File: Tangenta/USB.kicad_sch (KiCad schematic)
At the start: 29 parts, among them J12 907-211A1019D10200, J13 906-151A1058D10200, U8 USB2514B-I_M2, X1 X322524MOB4SI

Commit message: Libraries exported from global to project.
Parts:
- C1: symbol Device:C_Small -> CholaSymbolsPrjLib:C_Small
- C48, C49: symbol CAP_L5:16CE47FSS -> CholaSymbolsPrjLib:16CE47FSS
- FB1: symbol Ferrite_Bead_100:GZ2012D101TF -> CholaSymbolsPrjLib:GZ2012D101TF
- J12: symbol USB_2_CONNECTOR:907-211A1019D10200 -> CholaSymbolsPrjLib:907-211A1019D10200
- J13: symbol USB_VERTICAL_BLUE:906-151A1058D10200 -> CholaSymbolsPrjLib:906-151A1058D10200
- R2: symbol Device:R_Small_US -> CholaSymbolsPrjLib:R_Small_US
- U8: symbol USB_HUB:USB2514B-I_M2 -> CholaSymbolsPrjLib:USB2514B-I_M2
- X1: symbol XTAL_24MHZ:X322524MOB4SI -> CholaSymbolsPrjLib:X322524MOB4SI
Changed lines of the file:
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@@
     (effects (font (size 1.27 1.27)) (justify right))
   )
-  (symbol (lib_id "Device:R_Small_US") (at 184.15 97.79 270) (mirror x) (unit 1)
+  (symbol (lib_id "CholaSymbolsPrjLib:R_Small_US") (at 184.15 97.79 270) (mirror x) (unit 1)
     (in_bom yes) (on_board yes) (dnp no)
     (property "Reference" "R2" (at 186.055 96.52 90)
@@
     )
   )
-  (symbol (lib_id "Device:C_Small") (at 62.611 168.91 180) (unit 1)
+  (symbol (lib_id "CholaSymbolsPrjLib:C_Small") (at 62.611 168.91 180) (unit 1)
     (in_bom yes) (on_board yes) (dnp no)
     (property "Reference" "C1" (at 60.452 167.386 0)
@@
     )
   )
-  (symbol (lib_id "Device:C_Small") (at 38.862 168.91 180) (unit 1)
+  (symbol (lib_id "CholaSymbolsPrjLib:C_Small") (at 38.862 168.91 180) (unit 1)
     (in_bom yes) (on_board yes) (dnp no)
     (property "Reference" "C1" (at 36.703 167.386 0)
@@
     )
   )
-  (symbol (lib_id "Device:C_Small") (at 55.118 168.91 180) (unit 1)
+  (symbol (lib_id "CholaSymbolsPrjLib:C_Small") (at 55.118 168.91 180) (unit 1)
     (in_bom yes) (on_board yes) (dnp no)
     (property "Reference" "C1" (at 52.959 167.386 0)
@@
     )
   )
-  (symbol (lib_id "XTAL_24MHZ:X322524MOB4SI") (at 104.775 166.37 180) (unit 1)
+  (symbol (lib_id "CholaSymbolsPrjLib:X322524MOB4SI") (at 104.775 166.37 180) (unit 1)
     (in_bom yes) (on_board yes) (dnp no)
     (property "Reference" "X1" (at 104.775 160.02 0)
@@
     )
   )
-  (symbol (lib_id "Device:C_Small") (at 46.355 168.91 180) (unit 1)
+  (symbol (lib_id "CholaSymbolsPrjLib:C_Small") (at 46.355 168.91 180) (unit 1)
     (in_bom yes) (on_board yes) (dnp no)
     (property "Reference" "C1" (at 44.196 167.386 0)
@@
     )
   )
-  (symbol (lib_id "Device:C_Small") (at 95.25 180.34 180) (unit 1)
+  (symbol (lib_id "CholaSymbolsPrjLib:C_Small") (at 95.25 180.34 180) (unit 1)
     (in_bom yes) (on_board yes) (dnp no)
     (property "Reference" "C1" (at 99.06 180.34 0)
@@
     )
   )
-  (symbol (lib_id "Device:C_Small") (at 33.655 66.04 180) (unit 1)
+  (symbol (lib_id "CholaSymbolsPrjLib:C_Small") (at 33.655 66.04 180) (unit 1)
     (in_bom yes) (on_board yes) (dnp no)
     (property "Reference" "C1" (at 36.195 64.135 0)
@@
     )
   )
-  (symbol (lib_id "Device:R_Small_US") (at 60.96 77.47 90) (unit 1)
+  (symbol (lib_id "CholaSymbolsPrjLib:R_Small_US") (at 60.96 77.47 90) (unit 1)
     (in_bom yes) (on_board yes) (dnp no)
     (property "Reference" "R2" (at 59.055 76.2 90)
@@
     )
   )
-  (symbol (lib_id "USB_HUB:USB2514B-I_M2") (at 118.1101 76.2 0) (mirror y) (unit 1)
+  (symbol (lib_id "CholaSymbolsPrjLib:USB2514B-I_M2") (at 118.1101 76.2 0) (mirror y) (unit 1)
     (in_bom yes) (on_board yes) (dnp no)
     (property "Reference" "U8" (at 74.93 50.165 0)
@@
     )
   )
-  (symbol (lib_id "Device:R_Small_US") (at 60.96 100.33 90) (unit 1)
+  (symbol (lib_id "CholaSymbolsPrjLib:R_Small_US") (at 60.96 100.33 90) (unit 1)
     (in_bom yes) (on_board yes) (dnp no)
     (property "Reference" "R2" (at 59.182 99.06 90)
@@
     )
   )
-  (symbol (lib_id "Device:C_Small") (at 206.375 93.98 180) (unit 1)
+  (symbol (lib_id "CholaSymbolsPrjLib:C_Small") (at 206.375 93.98 180) (unit 1)
     (in_bom yes) (on_board yes) (dnp no)
     (property "Reference" "C1" (at 208.915 92.075 0)
@@
     )
   )
-  (symbol (lib_id "Device:R_Small_US") (at 60.96 95.25 90) (unit 1)
+  (symbol (lib_id "CholaSymbolsPrjLib:R_Small_US") (at 60.96 95.25 90) (unit 1)
     (in_bom yes) (on_board yes) (dnp no)
     (property "Reference" "R2" (at 59.182 93.98 90)
@@
     )
   )
-  (symbol (lib_id "USB_2_CONNECTOR:907-211A1019D10200") (at 268.605 64.77 0) (unit 1)
+  (symbol (lib_id "CholaSymbolsPrjLib:907-211A1019D10200") (at 268.605 64.77 0) (unit 1)
     (in_bom yes) (on_board yes) (dnp no)
     (property "Reference" "J12" (at 258.445 50.165 0)
@@
     )
   )
-  (symbol (lib_id "Device:R_Small_US") (at 183.515 87.63 270) (mirror x) (unit 1)
+  (symbol (lib_id "CholaSymbolsPrjLib:R_Small_US") (at 183.515 87.63 270) (mirror x) (unit 1)
     (in_bom yes) (on_board yes) (dnp no)
     (property "Reference" "R2" (at 185.42 86.36 90)
@@
     )
   )
-  (symbol (lib_id "Device:C_Small") (at 114.3 180.34 180) (unit 1)
+  (symbol (lib_id "CholaSymbolsPrjLib:C_Small") (at 114.3 180.34 180) (unit 1)
     (in_bom yes) (on_board yes) (dnp no)
     (property "Reference" "C1" (at 110.49 180.34 0)
@@
     )
   )
-  (symbol (lib_id "Ferrite_Bead_100:GZ2012D101TF") (at 50.673 163.83 0) (unit 1)
+  (symbol (lib_id "CholaSymbolsPrjLib:GZ2012D101TF") (at 50.673 163.83 0) (unit 1)
     (in_bom yes) (on_board yes) (dnp no)
     (property "Reference" "FB1" (at 50.673 161.29 0)
@@
     )
   )
-  (symbol (lib_id "USB_VERTICAL_BLUE:906-151A1058D10200") (at 266.7 93.98 0) (unit 1)
+  (symbol (lib_id "CholaSymbolsPrjLib:906-151A1058D10200") (at 266.7 93.98 0) (unit 1)
     (in_bom yes) (on_board yes) (dnp no)
     (property "Reference" "J13" (at 260.35 85.09 0)
@@
     )
   )
-  (symbol (lib_id "CAP_L5:16CE47FSS") (at 62.103 187.071 0) (unit 1)
+  (symbol (lib_id "CholaSymbolsPrjLib:16CE47FSS") (at 62.103 187.071 0) (unit 1)
     (in_bom yes) (on_board yes) (dnp no)
     (property "Reference" "C48" (at 62.357 185.42 0)
@@
     )
   )
-  (symbol (lib_id "Device:R_Small_US") (at 105.41 177.8 90) (unit 1)
+  (symbol (lib_id "CholaSymbolsPrjLib:R_Small_US") (at 105.41 177.8 90) (unit 1)
     (in_bom yes) (on_board yes) (dnp no)
     (property "Reference" "R2" (at 103.505 176.53 90)
@@
     )
   )
-  (symbol (lib_id "CAP_L5:16CE47FSS") (at 70.104 187.071 0) (unit 1)
+  (symbol (lib_id "CholaSymbolsPrjLib:16CE47FSS") (at 70.104 187.071 0) (unit 1)
     (in_bom yes) (on_board yes) (dnp no)
     (property "Reference" "C49" (at 70.358 185.42 0)
@@
     )
   )
-  (symbol (lib_id "Device:C_Small") (at 201.295 93.98 180) (unit 1)
+  (symbol (lib_id "CholaSymbolsPrjLib:C_Small") (at 201.295 93.98 180) (unit 1)
     (in_bom yes) (on_board yes) (dnp no)
     (property "Reference" "C1" (at 198.755 92.075 0)
@@
     )
   )
-  (symbol (lib_id "Device:C_Small") (at 70.104 168.91 180) (unit 1)
+  (symbol (lib_id "CholaSymbolsPrjLib:C_Small") (at 70.104 168.91 180) (unit 1)
     (in_bom yes) (on_board yes) (dnp no)
     (property "Reference" "C1" (at 67.945 167.386 0)
@@
     )
   )
-  (symbol (lib_id "Device:C_Small") (at 43.815 86.36 180) (unit 1)
+  (symbol (lib_id "CholaSymbolsPrjLib:C_Small") (at 43.815 86.36 180) (unit 1)
     (in_bom yes) (on_board yes) (dnp no)
     (property "Reference" "C1" (at 40.005 85.725 0)
@@
     )
   )
-  (symbol (lib_id "Device:C_Small") (at 28.575 66.04 180) (unit 1)
+  (symbol (lib_id "CholaSymbolsPrjLib:C_Small") (at 28.575 66.04 180) (unit 1)
     (in_bom yes) (on_board yes) (dnp no)
     (property "Reference" "C1" (at 26.035 64.135 0)
@@
     )
   )
-  (symbol (lib_id "Device:R_Small_US") (at 60.96 59.69 90) (unit 1)
+  (symbol (lib_id "CholaSymbolsPrjLib:R_Small_US") (at 60.96 59.69 90) (unit 1)
     (in_bom yes) (on_board yes) (dnp no)
     (property "Reference" "R2" (at 59.055 58.42 90)
@@
     )
   )
-  (symbol (lib_id "Device:R_Small_US") (at 60.96 85.09 90) (unit 1)
+  (symbol (lib_id "CholaSymbolsPrjLib:R_Small_US") (at 60.96 85.09 90) (unit 1)
     (in_bom yes) (on_board yes) (dnp no)
     (property "Reference" "R2" (at 59.055 83.82 90)
@@
     )
   )
-  (symbol (lib_id "Device:R_Small_US") (at 40.005 82.55 90) (unit 1)
+  (symbol (lib_id "CholaSymbolsPrjLib:R_Small_US") (at 40.005 82.55 90) (unit 1)
     (in_bom yes) (on_board yes) (dnp no)
     (property "Reference" "R2" (at 38.1 81.28 90)
@@
     )
   )
-  (symbol (lib_id "Device:C_Small") (at 31.369 168.91 180) (unit 1)
+  (symbol (lib_id "CholaSymbolsPrjLib:C_Small") (at 31.369 168.91 180) (unit 1)
     (in_bom yes) (on_board yes) (dnp no)
     (property "Reference" "C1" (at 29.21 167.386 0)

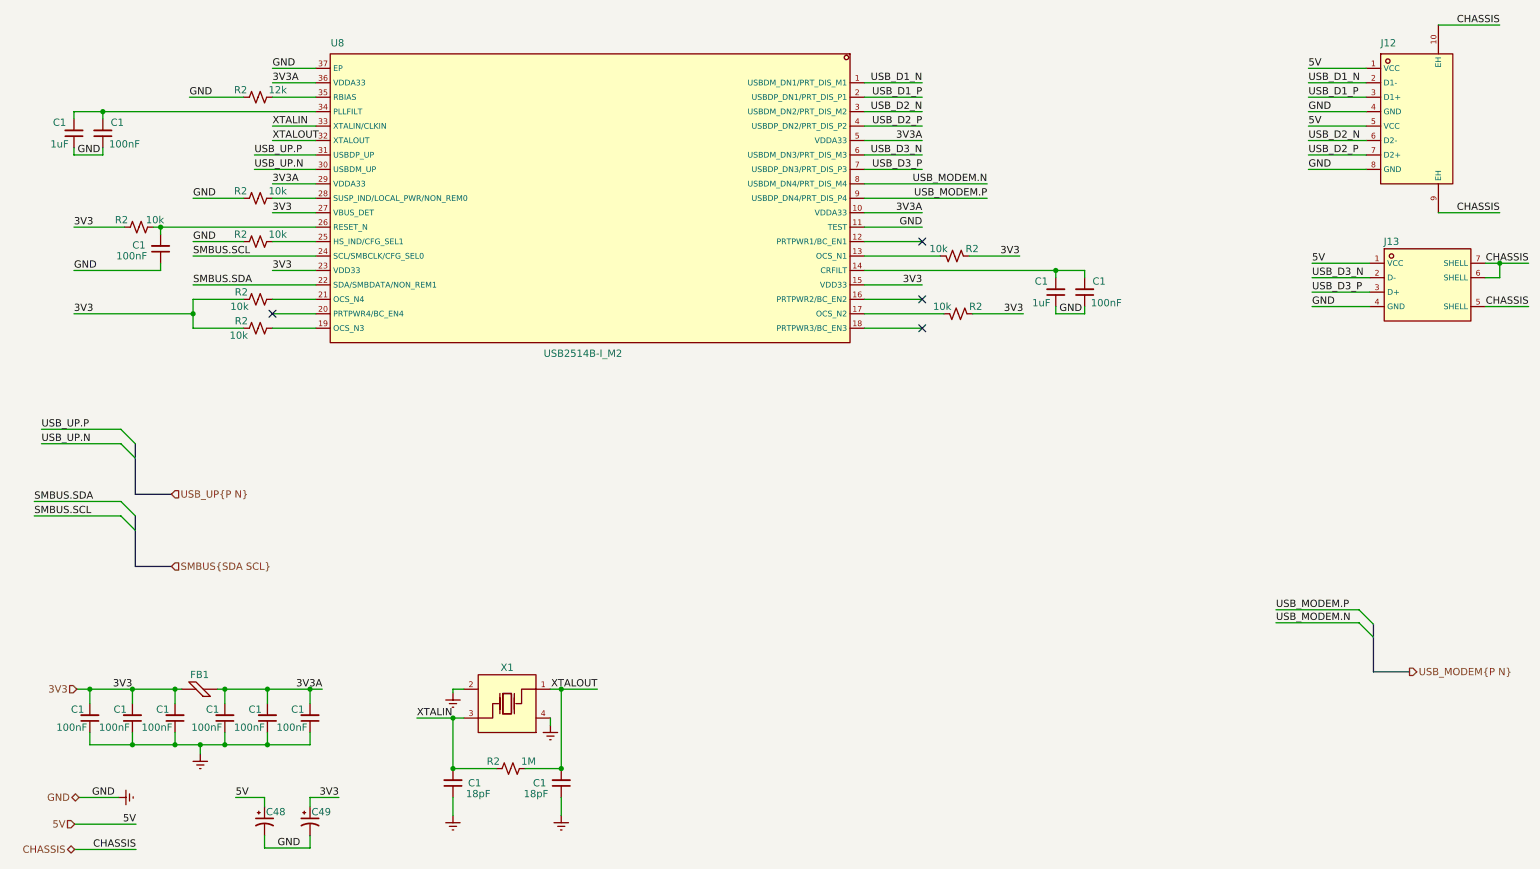
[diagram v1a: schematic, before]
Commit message: Re-annotated. Ready for JLCPCB design verification.
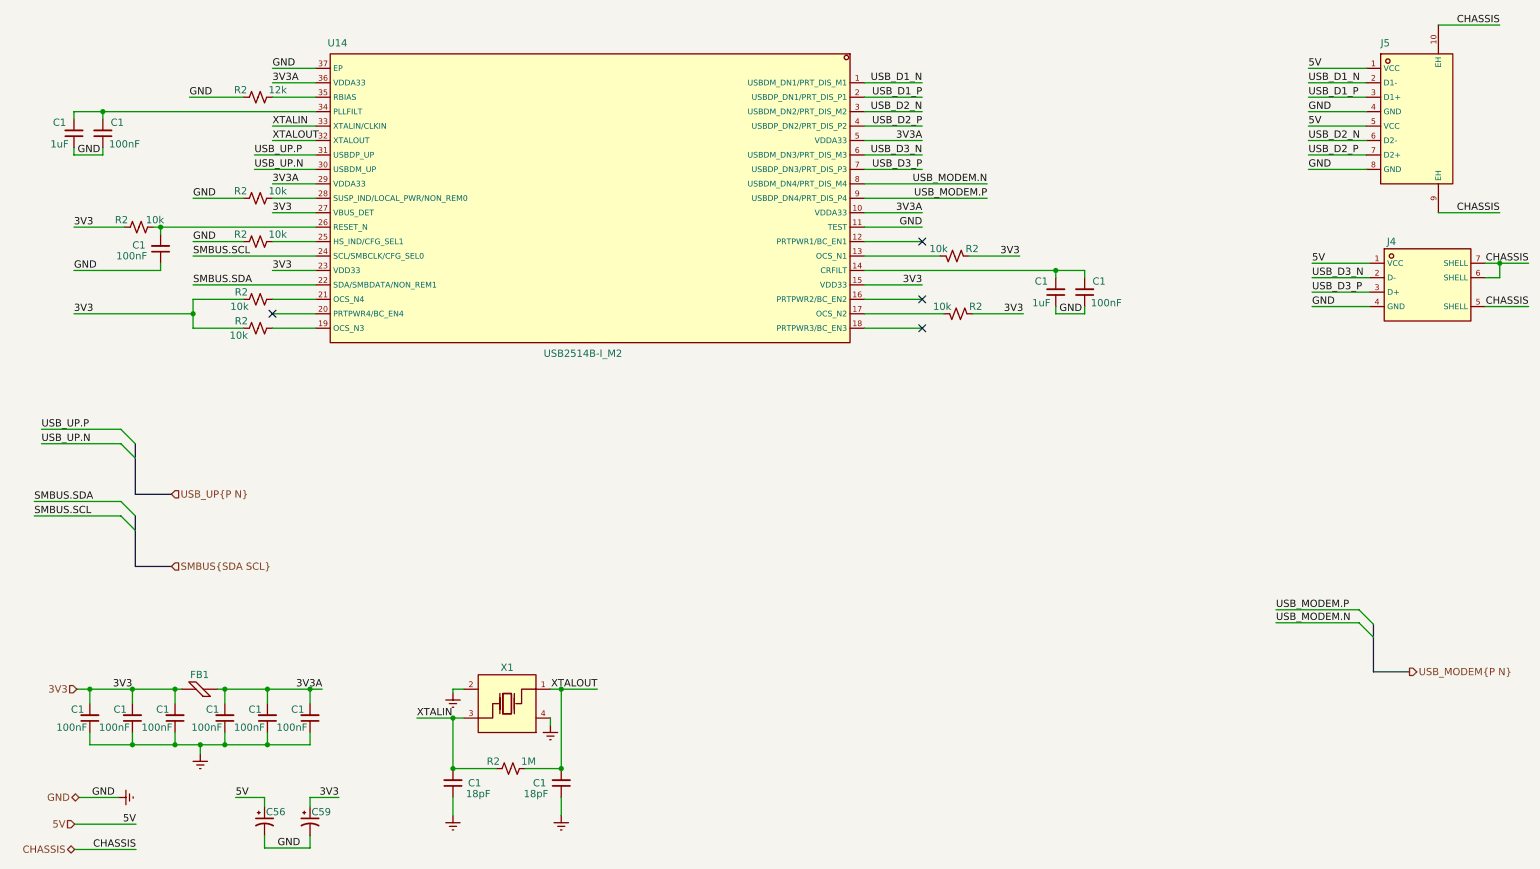
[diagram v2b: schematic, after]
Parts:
- renumbered C48 to C56, C49 to C59, J13 to J4, J12 to J5, U8 to U14

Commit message: initialize branch
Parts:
- renumbered C1 to C49, C1 to C50, C1 to C51, C1 to C52, C1 to C53, C1 to C54, C1 to C55, C1 to C57, C1 to C58, C1 to C60, C1 to C61, C1 to C62, C1 to C63, R2 to R33, R2 to R34, R2 to R35, R2 to R36, R2 to R37, R2 to R38, R2 to R39, R2 to R40, R2 to R41

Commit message: U14,J4,J5
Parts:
- J4: footprint USB_VERTICAL_BLUE:USB_VERTICAL_BLUE -> CholaFootprintsPrjLib:USB_VERTICAL_BLUE
- J5: footprint USB_2_CONNECTOR:USB_2_CONNECTOR -> CholaFootprintsPrjLib:USB_2_CONNECTOR
- U14: footprint USB_HUB:USB_HUB -> CholaFootprintsPrjLib:USB_HUB
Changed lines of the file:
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@@
       (effects (font (size 1.27 1.27)))
     )
-    (property "Footprint" "USB_HUB:USB_HUB" (at 156.2101 115.57 0)
+    (property "Footprint" "CholaFootprintsPrjLib:USB_HUB" (at 156.2101 115.57 0)
       (effects (font (size 1.27 1.27) italic) hide)
     )
@@
       (effects (font (size 1.27 1.27)) (justify left) hide)
     )
-    (property "Footprint" "USB_2_CONNECTOR:USB_2_CONNECTOR" (at 291.465 67.31 0)
+    (property "Footprint" "CholaFootprintsPrjLib:USB_2_CONNECTOR" (at 291.465 67.31 0)
       (effects (font (size 1.27 1.27) italic) hide)
     )
@@
       (effects (font (size 1.27 1.27)) hide)
     )
-    (property "Footprint" "USB_VERTICAL_BLUE:USB_VERTICAL_BLUE" (at 267.589 108.585 0)
-      (effects (font (size 1.27 1.27) italic) hide)
-    )
+    (property "Footprint" "CholaFootprintsPrjLib:USB_VERTICAL_BLUE" (at 267.589 108.585 0)
+      (effects (font (size 1.27 1.27) italic) hide)
+    )

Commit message: CAP_L5, CR2032_HOL, Ferrite_Bead, XTAL_24-25
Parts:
- FB1: footprint Ferrite_Bead_100:Ferrite_Bead_100 -> CholaFootprintsPrjLib:Ferrite_Bead_100
- X1: footprint XTAL_24MHZ:XTAL_24MHZ -> CholaFootprintsPrjLib:XTAL_24MHZ
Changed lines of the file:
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@@
       (effects (font (size 1.27 1.27)) hide)
     )
-    (property "Footprint" "XTAL_24MHZ:XTAL_24MHZ" (at 113.411 150.114 0)
+    (property "Footprint" "CholaFootprintsPrjLib:XTAL_24MHZ" (at 113.411 150.114 0)
       (effects (font (size 1.27 1.27) italic) hide)
     )
@@
       (effects (font (size 1.27 1.27)) hide)
     )
-    (property "Footprint" "Ferrite_Bead_100:Ferrite_Bead_100" (at 63.246 173.863 0)
+    (property "Footprint" "CholaFootprintsPrjLib:Ferrite_Bead_100" (at 63.246 173.863 0)
       (effects (font (size 1.27 1.27) italic) hide)
     )

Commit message: CAP_L5, NTZD3154NT1G
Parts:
- C56, C59: footprint CAP_L5:CAP_L5 -> CholaFootprintsPrjLib:CAP_L5
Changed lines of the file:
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@@
       (effects (font (size 1.27 1.27)) (justify left) hide)
     )
-    (property "Footprint" "CAP_L5:CAP_L5" (at 60.833 204.851 0)
+    (property "Footprint" "CholaFootprintsPrjLib:CAP_L5" (at 60.833 204.851 0)
       (effects (font (size 1.27 1.27) italic) hide)
     )
@@
     )
   )
-  (symbol (lib_id "CholaSymbolsPrjLib:16CE47FSS") (at 70.104 187.071 0) (unit 1)
+  (symbol (lib_name "16CE47FSS_1") (lib_id "CholaSymbolsPrjLib:16CE47FSS") (at 70.104 187.071 0) (unit 1)
     (in_bom yes) (on_board yes) (dnp no)
     (property "Reference" "C59" (at 70.358 185.42 0)
@@
       (effects (font (size 1.27 1.27)) (justify left) hide)
     )
-    (property "Footprint" "CAP_L5:CAP_L5" (at 68.834 204.851 0)
+    (property "Footprint" "CholaFootprintsPrjLib:CAP_L5" (at 68.834 204.851 0)
       (effects (font (size 1.27 1.27) italic) hide)
     )
